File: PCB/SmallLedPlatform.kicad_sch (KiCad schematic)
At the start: 33 parts, among them J101 USB_C_Receptacle, J102 Conn_02x05_Odd_Even, J103 Conn_01x03_Male, J104 Conn_01x03_Male, Q101 AO3400A, U101 STM32G0B1CBTx, U102 USBLC6-2P6, U103 TCPP01-M12

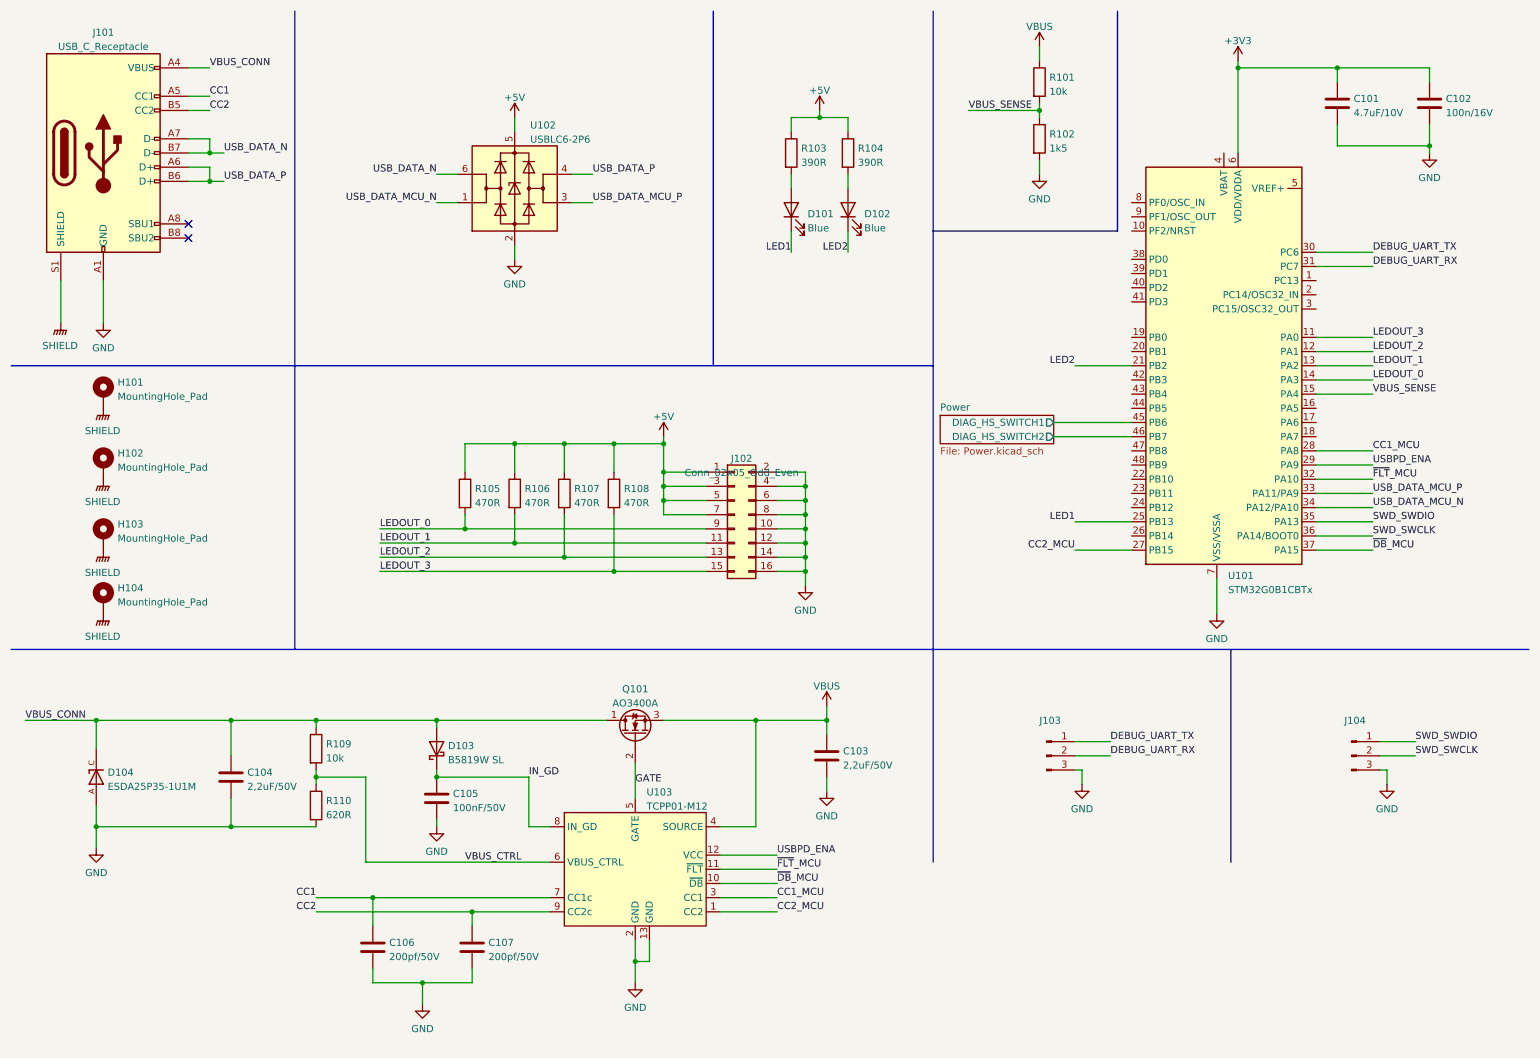
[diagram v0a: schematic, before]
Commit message: reroute pretty much everything
Routing is done for new DC/DC!
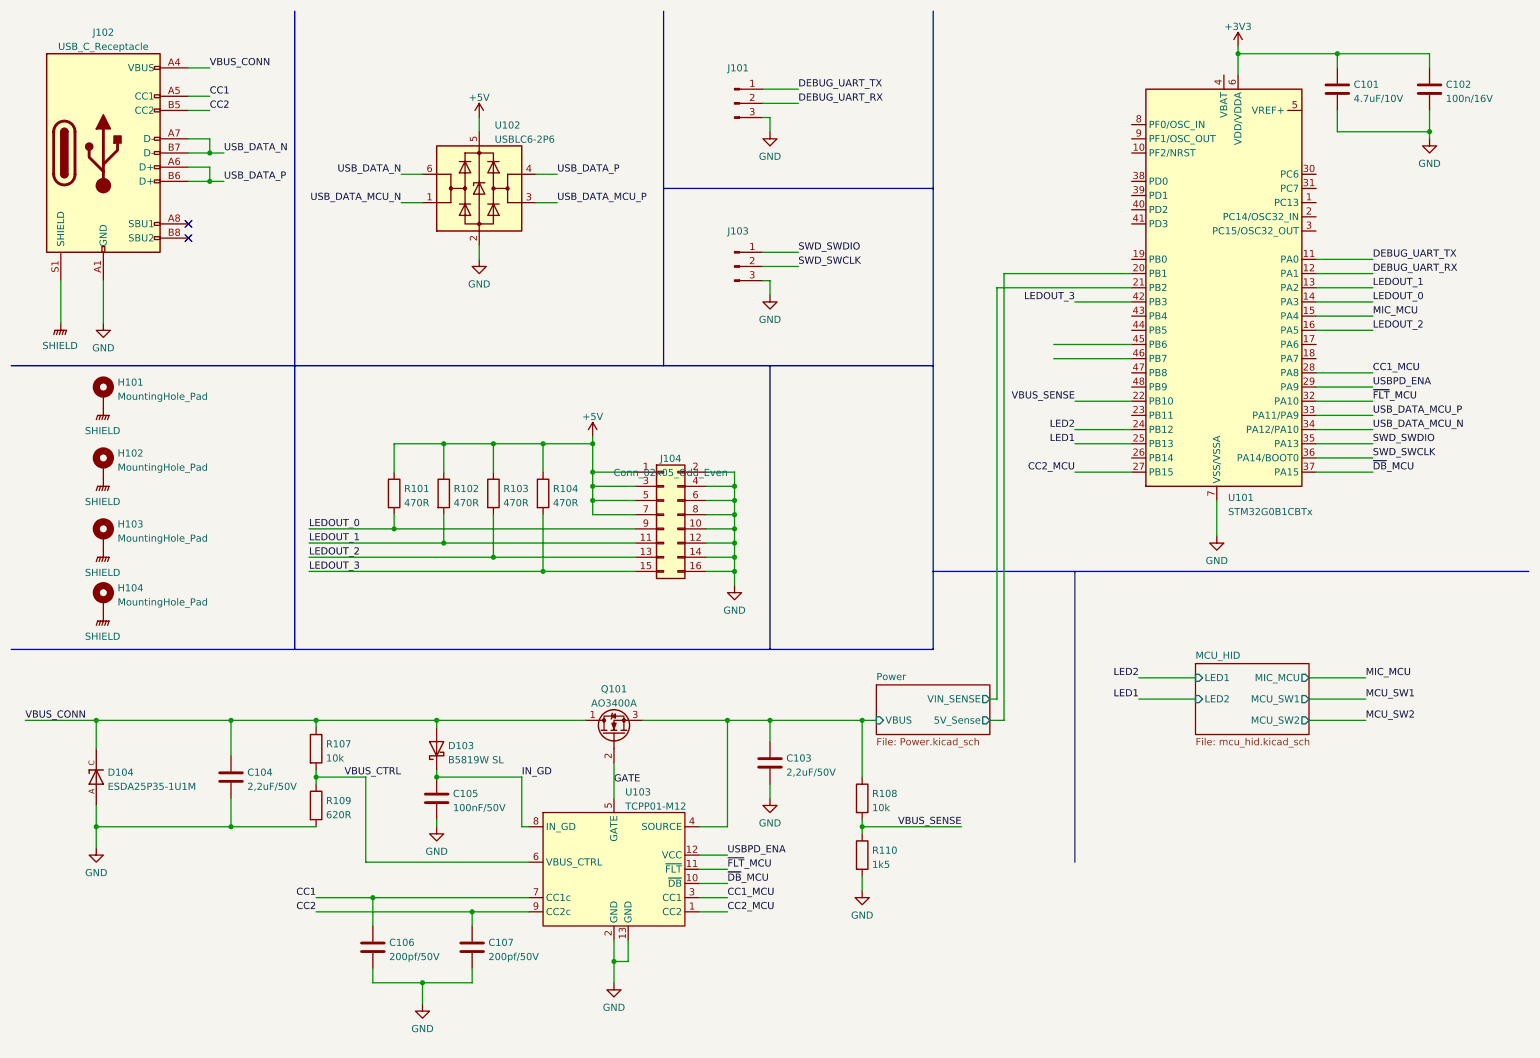
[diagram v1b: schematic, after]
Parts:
- removed D101, D102: Blue, LED_SMD:LED_0603_1608Metric, symbol Device:LED
- removed R101: 10k, Resistor_SMD:R_0402_1005Metric, symbol Device:R
- removed R102: 1k5, Resistor_SMD:R_0402_1005Metric, symbol Device:R
- removed R103, R104: 390R, Resistor_SMD:R_0603_1608Metric, symbol Device:R
- added R108: 10k, Resistor_SMD:R_0402_1005Metric, symbol Device:R
- added R110: 1k5, Resistor_SMD:R_0402_1005Metric, symbol Device:R
- renumbered J103 to J101, J101 to J102, J104 to J103, J102 to J104, R105 to R101, R106 to R102, R107 to R103, R108 to R104, R109 to R107, R110 to R109
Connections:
- net DEBUG_UART_RX: now also U101.12 (PA1); no longer U101.31 (PC7)
- net DEBUG_UART_TX: now also U101.11 (PA0); no longer U101.30 (PC6)
- net GND: now also R110.2
- net LED2: now also U101.24 (PB12); no longer U101.21 (PB2)
- net LEDOUT_2: now also U101.16 (PA5); no longer U101.12 (PA1)
- net LEDOUT_3: now also U101.42 (PB3); no longer U101.11 (PA0)
- net VBUS_SENSE: now also U101.22 (PB10), R108.2, R110.1; no longer U101.15 (PA4)
- net Power/5V_Sense: now reaches U101.20 (PB1)
- net Power/DIAG_HS_SWITCH1: no longer names the net of U101.45 (PB6)
- net Power/DIAG_HS_SWITCH2: no longer names the net of U101.46 (PB7)
- net VBUS renamed Power/VBUS
- net Power/VBUS: now also R108.1
- new net MIC_MCU: U101.15 (PA4)
- new net Power/VIN_SENSE: U101.21 (PB2)
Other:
- added sheet MCU_HID (mcu_hid.kicad_sch)
- sheet Power ports: added 5V_Sense, VBUS, VIN_SENSE; removed DIAG_HS_SWITCH1, DIAG_HS_SWITCH2
- moved on the sheet: C101, C102, C103, J101, J103, J104, Q101, R101, R102, R103, R104, U101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

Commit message: Add LEDs for each USBPD level and a microphone
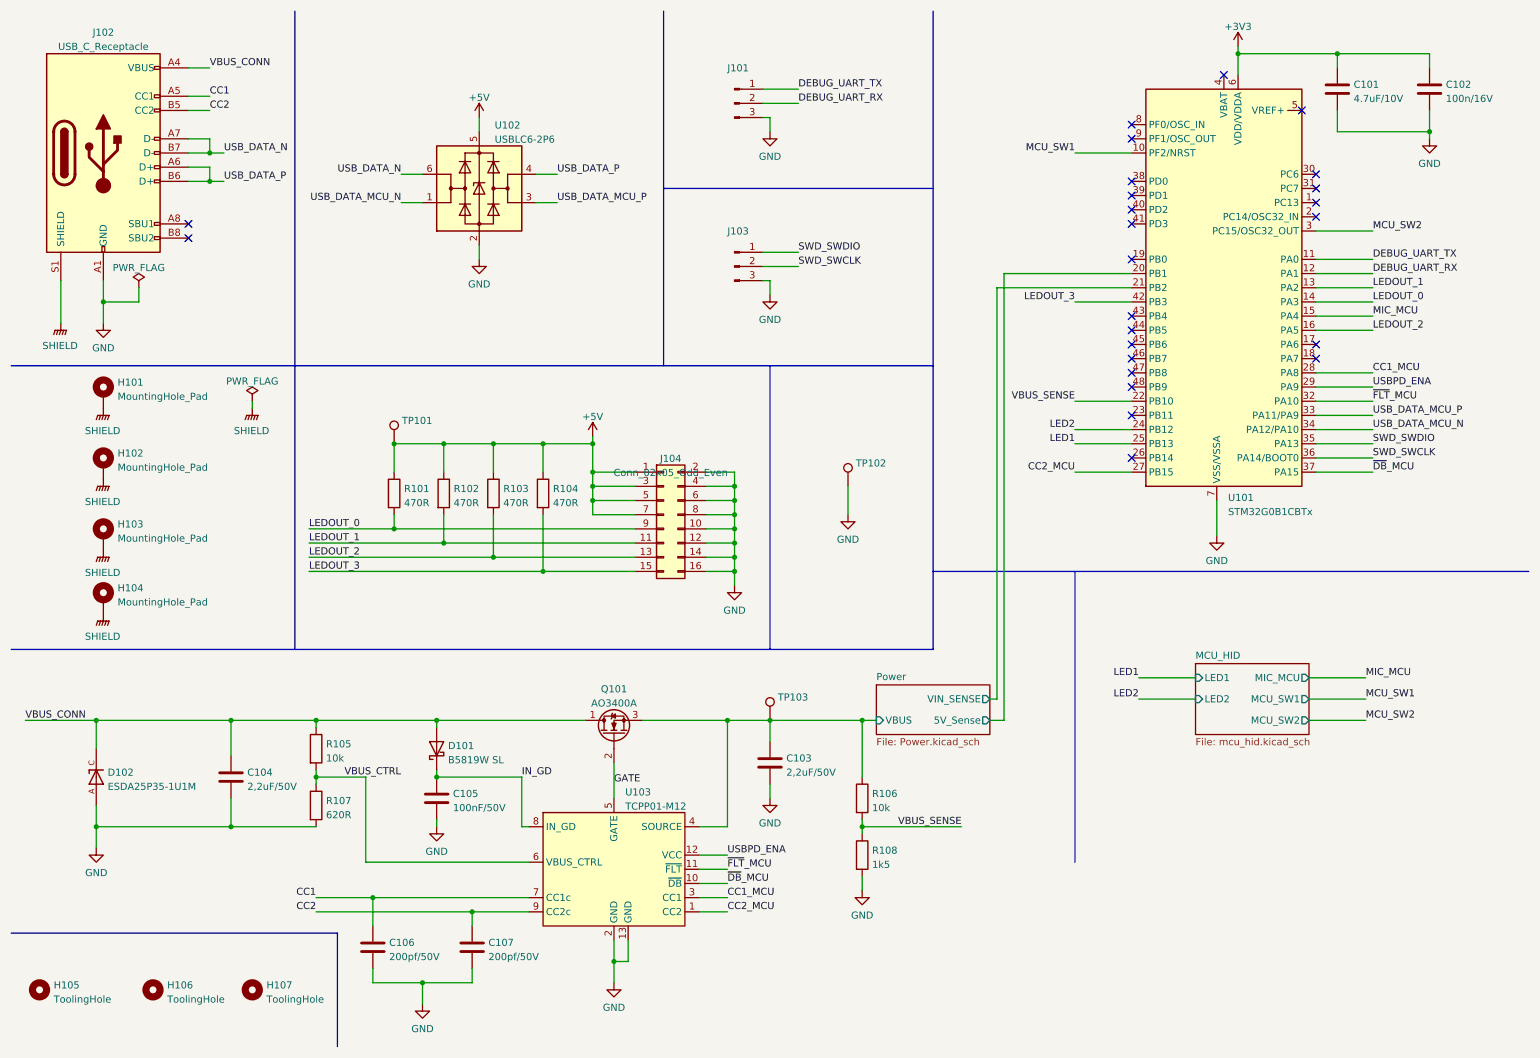
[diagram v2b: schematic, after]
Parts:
- added H105, H106, H107: ToolingHole, JLC:JLC_toolinghole, symbol Mechanical:MountingHole
- added TP101, TP102, TP103: TestPoint, TestPoint:TestPoint_Keystone_5000-5004_Miniature, symbol Connector:TestPoint
- J101, J103: LCSC (none) -> C49257
- J104: LCSC (none) -> C68234
- renumbered D103 to D101, D104 to D102, R107 to R105, R108 to R106, R109 to R107, R110 to R108
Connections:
- net +5V: now also TP101.1
- net GND: now also TP102.1
- net MCU_SW1: now also U101.10 (PF2/NRST)
- net MCU_SW2: now also U101.3 (PC15/OSC32_OUT)
- net Power/VBUS: now also TP103.1
- no-connect marks 2 -> 25

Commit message: Add fan header on backside of board
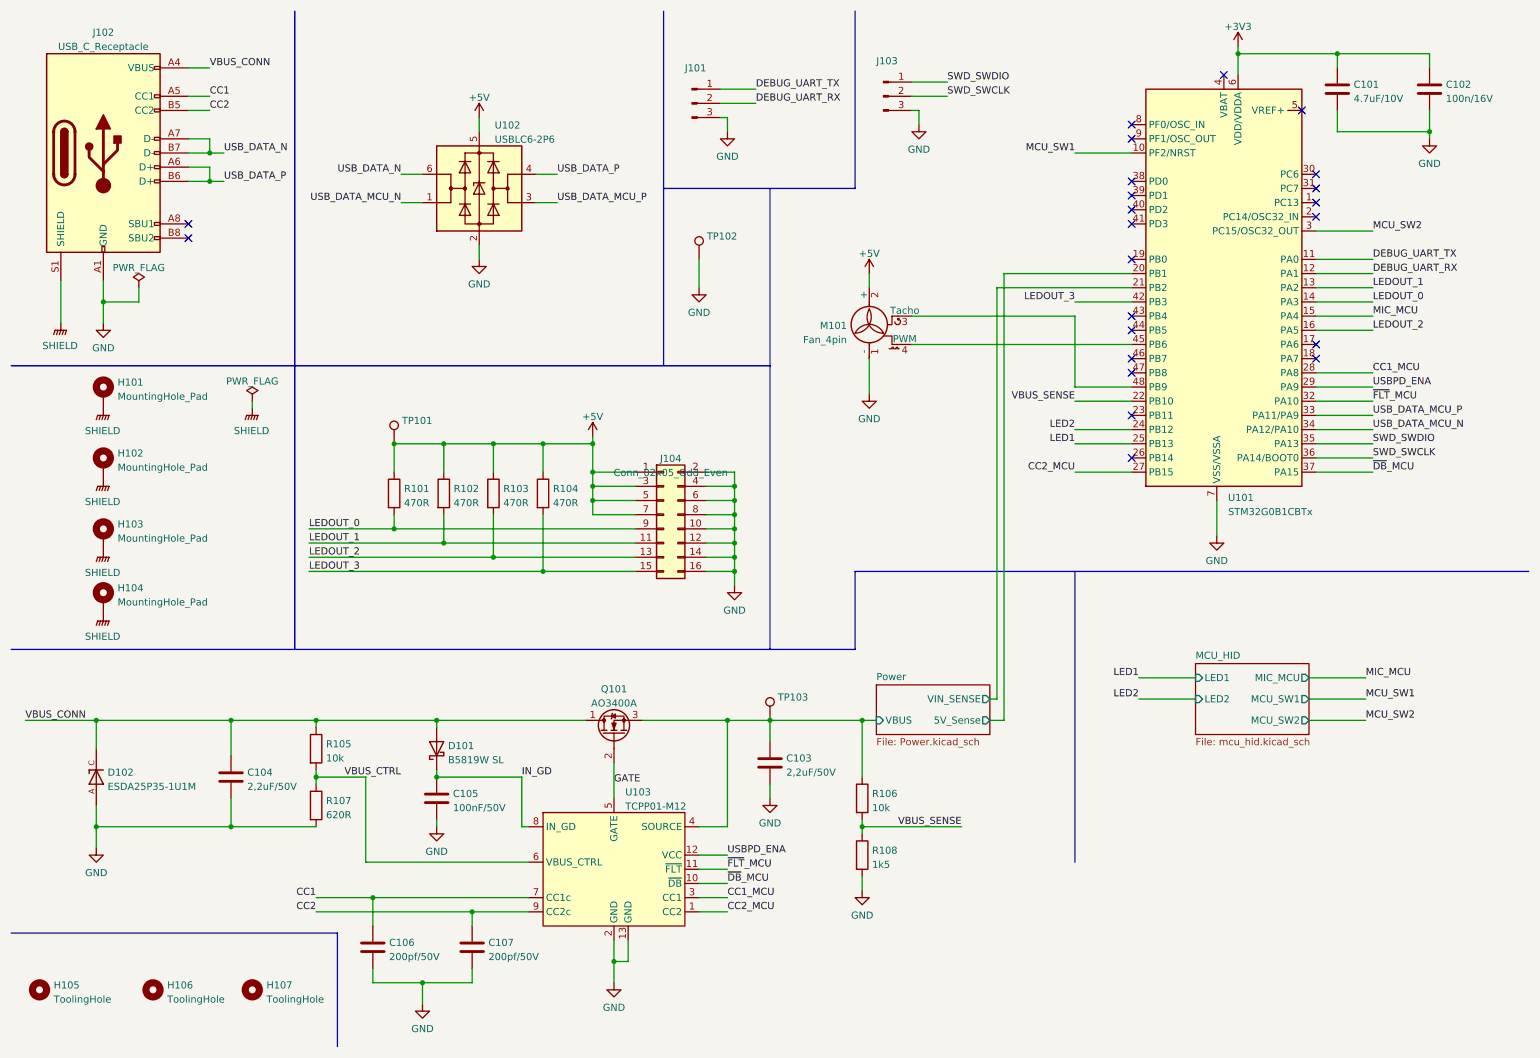
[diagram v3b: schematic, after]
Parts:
- added M101: Fan_4pin, Connector_PinHeader_2.54mm:PinHeader_1x04_P2.54mm_Vertical_SMD_Pin1Left, symbol Motor:Fan_4pin
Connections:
- net +5V: now also M101.2 (+)
- net GND: now also M101.1 (-)
- net at U101.45 (PB6): now also M101.4 (PWM)
- net at U101.48 (PB9): now also M101.3 (Tacho)
- no-connect marks 25 -> 23
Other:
- moved on the sheet: J101, J103, TP102

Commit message: Fix review comments
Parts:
- removed M101: Fan_4pin, Connector_PinHeader_2.54mm:PinHeader_1x04_P2.54mm_Vertical_SMD_Pin1Left, symbol Motor:Fan_4pin
- added C108: 100nF/50V, Capacitor_SMD:C_0402_1005Metric, symbol Device:C
- added C212: 1uF/25V, Capacitor_SMD:C_0402_1005Metric, symbol Device:C
- U101: symbol Skrooter_symbols:STM32G0B1CBTx -> Skrooterlib:STM32G0B1CBTx
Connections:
- net +3V3: now also U101.4 (VBAT)
- net GND: now also C108.2, C212.2
- net Fan_Tachomenter: now reaches U101.48 (PB9)
- net Fan_PWM: now reaches U101.45 (PB6)
- net HS_EN: now reaches U101.44 (PB5)
- net VREF+: now reaches U101.5 (VREF+)
- net VREF+: now also C108.1, C212.1
- net Power/5V_Sense renamed 5V_Sense
- net Power/VIN_SENSE renamed VIN_Sense
- no-connect marks 23 -> 20
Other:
- sheet MCU_HID ports: added Fan_PWM, Fan_Tachometer; removed none
- sheet Power ports: added ~{HSW_EN}; removed none
- moved on the sheet: C101, C102, J103, TP102, TP103, U101
